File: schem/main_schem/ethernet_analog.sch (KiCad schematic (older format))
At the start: 11 parts, among them U1 SPDT_ANALOG, U2 SPDT_ANALOG

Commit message: save schematics
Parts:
- added J1: RJ45-QEL, symbol RJ45-QEL
- added R22, R23: 220, symbol R
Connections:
- net +3.3V: now also J1.1 (TCT)
- net RX+: now also J1.4 (RD+)
- net RX-: now also J1.5 (RD-)
- net TX+: now also J1.2 (TD+)
- net TX-: now also J1.3 (TD-)
- net VSS: now also J1.7 (LEDG_K), J1.9 (LEDY_K)
- new net: J1.10 (LEDY_A), R23.2
- new net: J1.8 (LEDG_A), R22.2
- new net NET_LED_A: R22.1
- new net NET_LED_B: R23.1
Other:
- note added: "08B0-1G1T-06-F"
- moved on the sheet: R3
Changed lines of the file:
@@
-EESchema Schematic File Version 2  date 10/17/2012 8:53:55 AM
+EESchema Schematic File Version 2  date 10/20/2012 6:17:28 PM
 LIBS:power
 LIBS:device
@@
 Sheet 2 6
 Title "Ethernet Analog Subsystem w/ Polarity Switching"
-Date "17 oct 2012"
+Date "20 oct 2012"
 Rev ""
 Comp "Ingersoll Rand 402 Group"
@@
 Comment4 ""
 $EndDescr
-Wire Notes Line
-	1150 6700 10600 6700
+Wire Wire Line
+	4630 7540 4650 7540
+Wire Wire Line
+	4650 7340 4630 7340
+Connection ~ 5080 7640
+Wire Wire Line
+	5160 7640 5080 7640
+Wire Wire Line
+	5070 7040 5030 7040
+Wire Wire Line
+	5070 7040 5070 6940
+Wire Wire Line
+	5070 6940 5160 6940
+Wire Wire Line
+	5030 7040 5030 7120
+Wire Wire Line
+	5030 7120 4280 7120
+Wire Wire Line
+	4270 6740 5160 6740
+Wire Notes Line
+	1150 7800 1150 500
 Wire Notes Line
 	10600 2850 1150 2850
@@
 	9300 5100 6600 5100
 Wire Wire Line
-	7050 5700 6850 5700
-Wire Wire Line
-	6850 5700 6850 5800
+	7000 5500 6800 5500
+Wire Wire Line
+	6800 5500 6800 5600
 Wire Wire Line
 	6600 4700 7050 4700
@@
 	6600 3550 7050 3550
 Wire Wire Line
-	6850 6300 6850 6450
+	6800 6100 6800 6250
 Wire Wire Line
 	6600 3950 9300 3950
@@
 Connection ~ 9300 4250
 Wire Wire Line
-	5200 4300 2550 4300
-Wire Wire Line
-	4800 4500 2550 4500
+	2550 4300 5200 4300
+Wire Wire Line
+	2550 4500 4800 4500
 Wire Wire Line
 	4800 5100 5200 5100
@@
 Connection ~ 8000 1850
 Wire Notes Line
-	1150 6700 1150 500
-Wire Notes Line
 	1150 500  10600 500
 Wire Notes Line
 	10600 500  10600 6700
+Wire Notes Line
+	1150 6400 10600 6400
+Wire Wire Line
+	4270 6570 5020 6570
+Wire Wire Line
+	5020 6570 5020 6640
+Wire Wire Line
+	5020 6640 5160 6640
+Wire Wire Line
+	5030 6910 5030 6840
+Wire Wire Line
+	5030 6910 4270 6910
+Wire Wire Line
+	4280 7270 5070 7270
+Wire Wire Line
+	5070 7270 5070 7140
+Wire Wire Line
+	5070 7140 5160 7140
+Wire Wire Line
+	5030 6840 5160 6840
+Wire Wire Line
+	5160 7440 5080 7440
+Wire Wire Line
+	5080 7440 5080 7700
+Wire Wire Line
+	5150 7340 5160 7340
+Wire Wire Line
+	5160 7540 5150 7540
+Text GLabel 4630 7540 0    30   Input ~ 0
+NET_LED_B
+$Comp
+L R R23
+U 1 1 5082E53A
+P 4900 7540
+F 0 "R23" V 4820 7580 50  0000 C CNN
+F 1 "220" V 4900 7540 50  0000 C CNN
+	1    4900 7540
+	0    -1   -1   0
+$EndComp
+$Comp
+L R R22
+U 1 1 5082E45D
+P 4900 7340
+F 0 "R22" V 4820 7370 50  0000 C CNN
+F 1 "220" V 4900 7340 50  0000 C CNN
+	1    4900 7340
+	0    -1   -1   0
+$EndComp
+Text GLabel 4630 7340 0    30   Input ~ 0
+NET_LED_A
+Text Notes 6230 7770 0    30   ~ 0
+08B0-1G1T-06-F
+$Comp
+L VSS #PWR3
+U 1 1 5082E2BE
+P 5080 7700
+F 0 "#PWR3" H 5080 7700 30  0001 C CNN
+F 1 "VSS" H 5080 7630 30  0000 C CNN
+	1    5080 7700
+	1    0    0    -1
+$EndComp
+Text GLabel 4280 7120 0    60   Output ~ 0
+RX+
+Text GLabel 4280 7270 0    60   Output ~ 0
+RX-
+Text GLabel 4270 6570 0    60   Input ~ 0
+TX+
+Text GLabel 4270 6910 0    60   Input ~ 0
+TX-
+Text GLabel 4270 6740 0    60   Input ~ 0
+TXC
+$Comp
+L RJ45-QEL J1
+U 1 1 5082E1D8
+P 6260 7140
+F 0 "J1" H 6360 7740 60  0000 L CNN
+F 1 "RJ45-QEL" H 6210 7740 60  0000 R CNN
+	1    6260 7140
+	1    0    0    -1
+$EndComp
 Text Notes 1500 750  0    60   ~ 0
 ETHERNET RX
@@
 ETHERNET TX
 $Comp
-L +3.3V #PWR01
+L +3.3V #PWR1
 U 1 1 507229A7
 P 2950 1300
-F 0 "#PWR01" H 2950 1260 30  0001 C CNN
+F 0 "#PWR1" H 2950 1260 30  0001 C CNN
 F 1 "+3.3V" H 2950 1410 30  0000 C CNN
 	1    2950 1300
@@
 This is supposed to go to cener tap of transformer
 $Comp
-L VSS #PWR02
+L VSS #PWR9
 U 1 1 506EFD34
 P 7150 2500
-F 0 "#PWR02" H 7150 2500 30  0001 C CNN
+F 0 "#PWR9" H 7150 2500 30  0001 C CNN
 F 1 "VSS" H 7150 2430 30  0000 C CNN
 	1    7150 2500
@@
 $EndComp
 $Comp
-L VSS #PWR03
+L VSS #PWR2
 U 1 1 506EFD0E
 P 3750 5750
-F 0 "#PWR03" H 3750 5750 30  0001 C CNN
+F 0 "#PWR2" H 3750 5750 30  0001 C CNN
 F 1 "VSS" H 3750 5680 30  0000 C CNN
 	1    3750 5750
@@
 $EndComp
 $Comp
-L VSS #PWR04
+L VSS #PWR6
 U 1 1 506EFADF
-P 6850 6450
-F 0 "#PWR04" H 6850 6450 30  0001 C CNN
-F 1 "VSS" H 6850 6380 30  0000 C CNN
-	1    6850 6450
+P 6800 6250
+F 0 "#PWR6" H 6800 6250 30  0001 C CNN
+F 1 "VSS" H 6800 6180 30  0000 C CNN
+	1    6800 6250
 	1    0    0    -1
 $EndComp
@@
 L R R3
 U 1 1 506EFAD8
-P 6850 6050
-F 0 "R3" V 6930 6050 50  0000 C CNN
-F 1 "100k" V 6850 6050 50  0000 C CNN
-	1    6850 6050
-	1    0    0    -1
-$EndComp
-Text GLabel 7050 5700 2    60   Input ~ 0
+P 6800 5850
+F 0 "R3" V 6880 5850 50  0000 C CNN
+F 1 "100k" V 6800 5850 50  0000 C CNN
+	1    6800 5850
+	1    0    0    -1
+$EndComp
+Text GLabel 7000 5500 2    60   Input ~ 0
 RXSWAP
 Text GLabel 7050 4700 2    60   Input ~ 0
@@
 RXSWAP
 $Comp
-L VSS #PWR05
+L VSS #PWR4
 U 1 1 506EFA1F
 P 5100 3800
-F 0 "#PWR05" H 5100 3800 30  0001 C CNN
+F 0 "#PWR4" H 5100 3800 30  0001 C CNN
 F 1 "VSS" H 5100 3730 30  0000 C CNN
 	1    5100 3800
@@
 $EndComp
 $Comp
-L VSS #PWR06
+L VSS #PWR5
 U 1 1 506EF9D4
 P 5100 4950
-F 0 "#PWR06" H 5100 4950 30  0001 C CNN
+F 0 "#PWR5" H 5100 4950 30  0001 C CNN
 F 1 "VSS" H 5100 4880 30  0000 C CNN
 	1    5100 4950
@@
 $EndComp
 $Comp
-L +3.3V #PWR07
+L +3.3V #PWR8
 U 1 1 506EF9AE
 P 6900 4900
-F 0 "#PWR07" H 6900 4860 30  0001 C CNN
+F 0 "#PWR8" H 6900 4860 30  0001 C CNN
 F 1 "+3.3V" H 6900 5010 30  0000 C CNN
 	1    6900 4900
@@
 $EndComp
 $Comp
-L +3.3V #PWR08
+L +3.3V #PWR7
 U 1 1 506EF99F
 P 6900 3750
-F 0 "#PWR08" H 6900 3710 30  0001 C CNN
+F 0 "#PWR7" H 6900 3710 30  0001 C CNN
 F 1 "+3.3V" H 6900 3860 30  0000 C CNN
 	1    6900 3750

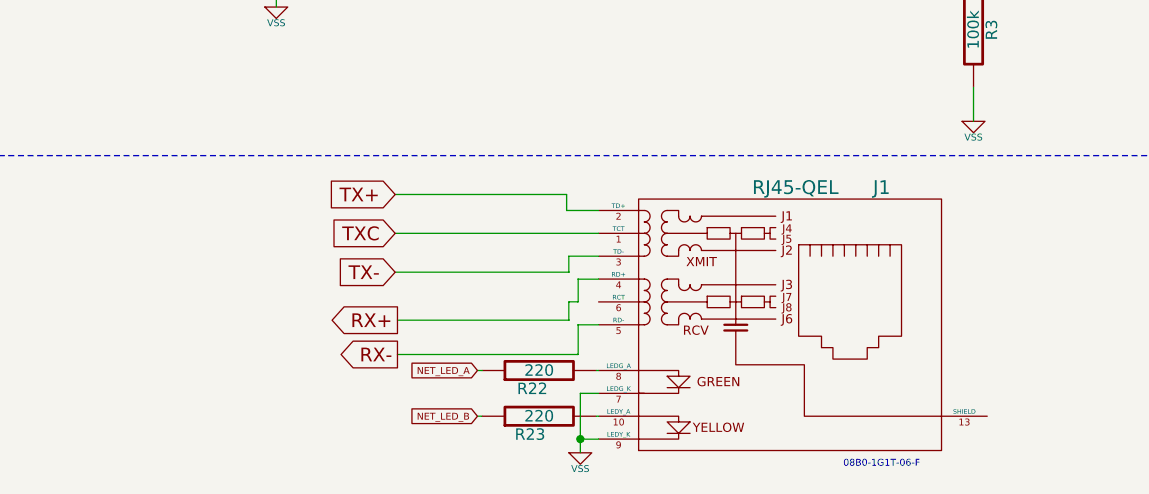
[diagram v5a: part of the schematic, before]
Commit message: Shielding pin for RJ45 jack, not connected to anything
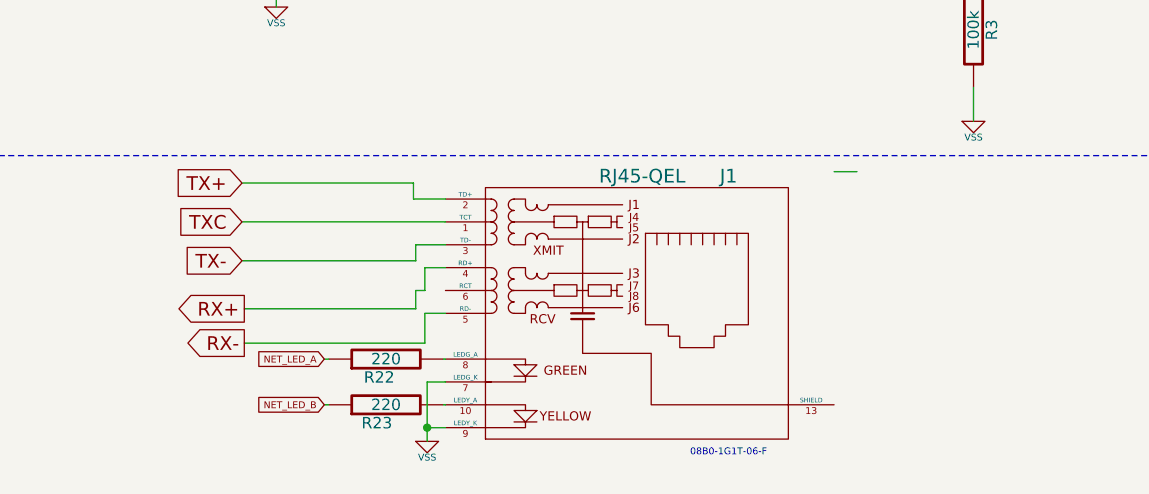
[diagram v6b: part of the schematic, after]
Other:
- moved on the sheet: J1, R22, R23
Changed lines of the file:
@@
-EESchema Schematic File Version 2  date 10/26/2012 9:37:13 AM
+EESchema Schematic File Version 2  date 11/1/2012 8:24:50 AM
 LIBS:power
 LIBS:device
@@
 Sheet 2 6
 Title "Ethernet Analog Subsystem w/ Polarity Switching"
-Date "26 oct 2012"
+Date "1 nov 2012"
 Rev ""
 Comp "Ingersoll Rand 402 Group"
@@
 $EndDescr
 Wire Wire Line
-	4630 7540 4650 7540
-Wire Wire Line
-	4650 7340 4630 7340
-Connection ~ 5080 7640
-Wire Wire Line
-	5160 7640 5080 7640
-Wire Wire Line
-	5070 7040 5030 7040
-Wire Wire Line
-	5070 7040 5070 6940
-Wire Wire Line
-	5070 6940 5160 6940
-Wire Wire Line
-	5030 7040 5030 7120
-Wire Wire Line
-	5030 7120 4280 7120
-Wire Wire Line
-	4270 6740 5160 6740
+	6290 6470 6190 6470
+Wire Wire Line
+	3960 7490 3980 7490
+Wire Wire Line
+	3980 7290 3960 7290
+Connection ~ 4410 7590
+Wire Wire Line
+	4490 7590 4410 7590
+Wire Wire Line
+	4400 6990 4360 6990
+Wire Wire Line
+	4400 6990 4400 6890
+Wire Wire Line
+	4400 6890 4490 6890
+Wire Wire Line
+	4360 6990 4360 7070
+Wire Wire Line
+	4360 7070 3610 7070
+Wire Wire Line
+	3600 6690 4490 6690
 Wire Notes Line
 	1150 7800 1150 500
@@
 	1150 6400 10600 6400
 Wire Wire Line
-	4270 6570 5020 6570
-Wire Wire Line
-	5020 6570 5020 6640
-Wire Wire Line
-	5020 6640 5160 6640
-Wire Wire Line
-	5030 6910 5030 6840
-Wire Wire Line
-	5030 6910 4270 6910
-Wire Wire Line
-	4280 7270 5070 7270
-Wire Wire Line
-	5070 7270 5070 7140
-Wire Wire Line
-	5070 7140 5160 7140
-Wire Wire Line
-	5030 6840 5160 6840
-Wire Wire Line
-	5160 7440 5080 7440
-Wire Wire Line
-	5080 7440 5080 7700
-Wire Wire Line
-	5150 7340 5160 7340
-Wire Wire Line
-	5160 7540 5150 7540
-Text GLabel 4630 7540 0    30   Input ~ 0
+	3600 6520 4350 6520
+Wire Wire Line
+	4350 6520 4350 6590
+Wire Wire Line
+	4350 6590 4490 6590
+Wire Wire Line
+	4360 6860 4360 6790
+Wire Wire Line
+	4360 6860 3600 6860
+Wire Wire Line
+	3610 7220 4400 7220
+Wire Wire Line
+	4400 7220 4400 7090
+Wire Wire Line
+	4400 7090 4490 7090
+Wire Wire Line
+	4360 6790 4490 6790
+Wire Wire Line
+	4490 7390 4410 7390
+Wire Wire Line
+	4410 7390 4410 7650
+Wire Wire Line
+	4480 7290 4490 7290
+Wire Wire Line
+	4490 7490 4480 7490
+Text GLabel 3960 7490 0    30   Input ~ 0
 NET_LED_B
 $Comp
 L R R23
 U 1 1 5082E53A
-P 4900 7540
-F 0 "R23" V 4820 7580 50  0000 C CNN
-F 1 "220" V 4900 7540 50  0000 C CNN
-	1    4900 7540
+P 4230 7490
+F 0 "R23" V 4150 7530 50  0000 C CNN
+F 1 "220" V 4230 7490 50  0000 C CNN
+	1    4230 7490
 	0    -1   -1   0
 $EndComp
@@
 L R R22
 U 1 1 5082E45D
-P 4900 7340
-F 0 "R22" V 4820 7370 50  0000 C CNN
-F 1 "220" V 4900 7340 50  0000 C CNN
-	1    4900 7340
+P 4230 7290
+F 0 "R22" V 4150 7320 50  0000 C CNN
+F 1 "220" V 4230 7290 50  0000 C CNN
+	1    4230 7290
 	0    -1   -1   0
 $EndComp
-Text GLabel 4630 7340 0    30   Input ~ 0
+Text GLabel 3960 7290 0    30   Input ~ 0
 NET_LED_A
-Text Notes 6230 7770 0    30   ~ 0
+Text Notes 5560 7720 0    30   ~ 0
 08B0-1G1T-06-F
 $Comp
 L VSS #PWR3
 U 1 1 5082E2BE
-P 5080 7700
-F 0 "#PWR3" H 5080 7700 30  0001 C CNN
-F 1 "VSS" H 5080 7630 30  0000 C CNN
-	1    5080 7700
-	1    0    0    -1
-$EndComp
-Text GLabel 4280 7120 0    60   Output ~ 0
+P 4410 7650
+F 0 "#PWR3" H 4410 7650 30  0001 C CNN
+F 1 "VSS" H 4410 7580 30  0000 C CNN
+	1    4410 7650
+	1    0    0    -1
+$EndComp
+Text GLabel 3610 7070 0    60   Output ~ 0
 RX+
-Text GLabel 4280 7270 0    60   Output ~ 0
+Text GLabel 3610 7220 0    60   Output ~ 0
 RX-
-Text GLabel 4270 6570 0    60   Input ~ 0
+Text GLabel 3600 6520 0    60   Input ~ 0
 TX+
-Text GLabel 4270 6910 0    60   Input ~ 0
+Text GLabel 3600 6860 0    60   Input ~ 0
 TX-
-Text GLabel 4270 6740 0    60   Input ~ 0
+Text GLabel 3600 6690 0    60   Input ~ 0
 TXC
 $Comp
 L RJ45-QEL J1
 U 1 1 5082E1D8
-P 6260 7140
-F 0 "J1" H 6360 7740 60  0000 L CNN
-F 1 "RJ45-QEL" H 6210 7740 60  0000 R CNN
-	1    6260 7140
+P 5590 7090
+F 0 "J1" H 5690 7690 60  0000 L CNN
+F 1 "RJ45-QEL" H 5540 7690 60  0000 R CNN
+	1    5590 7090
 	1    0    0    -1
 $EndComp
@@
 This is supposed to go to cener tap of transformer
 $Comp
-L VSS #PWR9
+L VSS #PWR10
 U 1 1 506EFD34
 P 7150 2500
-F 0 "#PWR9" H 7150 2500 30  0001 C CNN
+F 0 "#PWR10" H 7150 2500 30  0001 C CNN
 F 1 "VSS" H 7150 2430 30  0000 C CNN
 	1    7150 2500
@@
 $EndComp
 $Comp
-L VSS #PWR6
+L VSS #PWR7
 U 1 1 506EFADF
 P 6800 6250
-F 0 "#PWR6" H 6800 6250 30  0001 C CNN
+F 0 "#PWR7" H 6800 6250 30  0001 C CNN
 F 1 "VSS" H 6800 6180 30  0000 C CNN
 	1    6800 6250
@@
 $EndComp
 $Comp
-L +3.3V #PWR8
+L +3.3V #PWR9
 U 1 1 506EF9AE
 P 6900 4900
-F 0 "#PWR8" H 6900 4860 30  0001 C CNN
+F 0 "#PWR9" H 6900 4860 30  0001 C CNN
 F 1 "+3.3V" H 6900 5010 30  0000 C CNN
 	1    6900 4900
@@
 $EndComp
 $Comp
-L +3.3V #PWR7
+L +3.3V #PWR8
 U 1 1 506EF99F
 P 6900 3750
-F 0 "#PWR7" H 6900 3710 30  0001 C CNN
+F 0 "#PWR8" H 6900 3710 30  0001 C CNN
 F 1 "+3.3V" H 6900 3860 30  0000 C CNN
 	1    6900 3750
